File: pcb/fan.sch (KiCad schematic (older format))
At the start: 190 parts, among them J2 Pi, SW1 SW_PUSH, SW10 SW_PUSH, SW11 SW_PUSH, SW12 SW_PUSH, SW13 SW_PUSH, SW14 SW_PUSH, SW15 SW_PUSH, SW16 SW_PUSH, SW17 SW_PUSH, SW18 SW_PUSH, SW19 SW_PUSH, SW2 SW_PUSH, SW20 SW_PUSH, SW21 SW_PUSH, SW22 SW_PUSH, SW23 SW_PUSH, SW24 SW_PUSH, SW25 SW_PUSH, SW26 SW_PUSH, SW27 SW_PUSH, SW28 SW_PUSH, SW29 SW_PUSH, SW3 SW_PUSH, SW30 SW_PUSH, SW31 SW_PUSH, SW32 SW_PUSH, SW33 SW_PUSH, SW34 SW_PUSH, SW35 SW_PUSH, SW36 SW_PUSH, SW37 SW_PUSH, SW38 SW_PUSH, SW39 SW_PUSH, SW4 SW_PUSH, SW40 SW_PUSH, SW41 SW_PUSH, SW42 SW_PUSH, SW43 SW_PUSH, SW44 SW_PUSH, SW45 SW_PUSH, SW46 SW_PUSH, SW47 SW_PUSH, SW48 SW_PUSH, SW49 SW_PUSH, SW5 SW_PUSH, SW50 SW_PUSH, SW51 SW_PUSH, SW52 SW_PUSH, SW53 SW_PUSH, SW54 SW_PUSH, SW55 SW_PUSH, SW56 SW_PUSH, SW57 SW_PUSH, SW58 SW_PUSH, SW59 SW_PUSH, SW6 SW_PUSH, SW60 SW_PUSH, SW61 SW_PUSH, SW62 SW_PUSH, SW63 SW_PUSH, SW64 SW_PUSH, SW65 SW_PUSH, SW66 SW_PUSH, SW67 SW_PUSH, SW68 SW_PUSH, SW69 SW_PUSH, SW7 SW_PUSH, SW70 SW_PUSH, SW71 SW_PUSH, SW72 SW_PUSH, SW73 SW_PUSH, SW74 SW_PUSH, SW75 SW_PUSH, SW76 SW_PUSH, SW77 SW_PUSH, SW78 SW_PUSH, SW79 SW_PUSH, SW8 SW_PUSH, SW80 SW_PUSH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

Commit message: v2.0 外形考え中
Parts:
- removed D1, D10, D11, D12, D13, D14, D15, D16, D17, D18, D19, D2, D20, D21, D22, D23, D24, D25, D26, D27, D28, D29, D3, D30, D31, D32, D33, D34, D35, D36, D37, D38, D39, D4, D40, D41, D42, D43, D44, D45, D46, D47, D48, D49, D5, D50, D51, D52, D53, D54, D55, D56, D57, D58, D59, D6, D60, D61, D62, D63, D64, D65, D66, D67, D68, D69, D7, D70, D71, D72, D73, D74, D75, D76, D77, D78, D79, D8, D80, D81, D82, D83, D84, D85, D86, D87, D88, D89, D9, D90: DIODE, kbd:D3_TH_SMD, symbol Device:D
- removed J2: Pi, Connector_PinSocket_2.54mm:PinSocket_2x20_P2.54mm_Vertical, symbol fan-rescue:Connector_Generic_Conn_02x20_Odd_Even-Raspberry_Pi_Zero_W-cache
- removed SW1, SW10, SW11, SW12, SW13, SW14, SW15, SW16, SW17, SW18, SW19, SW2, SW20, SW21, SW22, SW23, SW24, SW25, SW26, SW27, SW28, SW29, SW3, SW30, SW31, SW32, SW33, SW34, SW35, SW36, SW37, SW38, SW39, SW4, SW40, SW41, SW42, SW43, SW44, SW45, SW46, SW47, SW48, SW5, SW51, SW52, SW53, SW54, SW56, SW57, SW58, SW59, SW6, SW60, SW61, SW62, SW63, SW64, SW65, SW66, SW67, SW68, SW69, SW7, SW70, SW71, SW72, SW73, SW74, SW75, SW76, SW77, SW78, SW79, SW8, SW80, SW81, SW82, SW83, SW84, SW85, SW86, SW87, SW88, SW89, SW9, SW90: SW_PUSH, kbd:CherryMX_Hotswap, symbol fan-rescue:SW_PUSH-kbd
- removed SW49, SW50, SW55: SW_PUSH, kbd:ResetSW, symbol fan-rescue:SW_PUSH-kbd
- removed SW93: SW_SPDT, Button_Switch_THT:SW_Slide_1P2T_CK_OS102011MS2Q, symbol Switch:SW_SPDT
- removed U4, U6: 74HC595, kbd:SN74HC595_DIP-16_W7.62mm_Socket_2, symbol 74xx:74HC595
- added SW1, SW11, SW12, SW13, SW14, SW16, SW17, SW18, SW19, SW2, SW20, SW21, SW22, SW23, SW24, SW25, SW26, SW27, SW28, SW29, SW3, SW30, SW31, SW32, SW33, SW34, SW35, SW36, SW37, SW38, SW39, SW4, SW40, SW6, SW7, SW8, SW9: SW_PUSH-kbd, kbd:CherryMX_MidHeight_Hotswap_edit, symbol New_Library:SW_PUSH-kbd
- added SW10, SW15, SW5: SW_PUSH-kbd, kbd:ResetSW_with_diode, symbol New_Library:SW_PUSH-kbd
- renumbered SW91 to SW41, SW92 to SW42
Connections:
- net labels removed: QHSER, QHSER', col08, col09, col10, col11, col12, col13, col14, row05
- wire segments 182 -> 80
- no-connect marks 58 -> 20

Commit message: 基盤の外形を決定した
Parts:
- added J1: MJ-4PP-9, kbd:MJ-4PP-9, symbol kbd:MJ-4PP-9
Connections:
- net labels added: data
- wire segments 80 -> 85
- no-connect marks 20 -> 18

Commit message: fan74をbluepillに変更
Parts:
- removed U1, U2: ProMicro, kbd:ProMicro_v3.6, symbol fan-rescue:ProMicro-kbd
- removed U3, U5: 74HC595, kbd:SN74HC595_DIP-16_W7.62mm_Socket_2, symbol 74xx:74HC595
- added R1: R, Resistor_THT:R_Axial_Power_L20.0mm_W6.4mm_P22.40mm, symbol Device:R
- added U1, U2: BluePill_STM32F103C, BluePill_breakouts:BluePill_STM32F103C, symbol bluepill_breakouts:BluePill_STM32F103C
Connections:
- net labels removed: OE, RCK, SCK, SCL, SER
- no-connect marks 18 -> 45
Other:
- moved on the sheet: SW42

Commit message: 配線にちょっと詰まったのでやり直す
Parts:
- added R10, R11, R12, R2, R20, R3, R4, R5, R6, R7, R8, R9: 10K, keyboard_parts:R_1608_rev2, symbol Device:R
- R1: value R -> 10K; footprint Resistor_THT:R_Axial_Power_L20.0mm_W6.4mm_P22.40mm -> keyboard_parts:R_1608_rev2
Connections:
- net data is gone; now on net Tx: J1.B
- net software_reset is gone; now on net hardware_reset: SW41.1
- net GND: now also SW42.1, U1.19 (GND), U1.20 (GND), U1.39 (GND), U2.19 (GND), U2.20 (GND), U2.39 (GND)
- net VCC: now also R1.2, U1.18 (VCC3V3), U1.40 (VCC3V3), U2.18 (VCC3V3), U2.40 (VCC3V3), R10.1, R11.1, R12.1, R2.1, R3.1, R4.1, R5.1, R6.1, R7.1, R8.1, R9.1; no longer R1.1
- net col01: now also U1.11 (PA6_MISO1), U2.11 (PA6_MISO1)
- net col02: now also U1.10 (PA5_SCK1), U2.10 (PA5_SCK1)
- net col03: now also U1.9 (PA4), U2.9 (PA4)
- net col04: now also U1.8 (PA3_RX2), U2.8 (PA3_RX2)
- net col05: now also U1.7 (PA2_TX2), U2.7 (PA2_TX2)
- net col06: now also U1.6 (PA1), U2.6 (PA1)
- net col07: now also U1.5 (PA0), U2.5 (PA0)
- net hardware_reset: now also U1.17 (NRST), U2.17 (NRST), R11.2; no longer SW42.1
- net row00: now also U1.33 (PB5), U2.33 (PB5)
- net row01: now also U1.34 (PB6_SCL1), U2.34 (PB6_SCL1)
- net row02: now also U1.35 (PB7_SDA1), U2.35 (PB7_SDA1)
- net row03: now also U1.36 (PB8), U2.36 (PB8)
- net row04: now also U1.37 (PB9), U2.37 (PB9)
- net at SW42.2: now also R12.2; no longer R1.2
- net PA7_R: now reaches U1.12 (PA7_MOSI1)
- net PA7_R: now also R1.1, U2.12 (PA7_MOSI1)
- net PB0_R: now reaches U1.13 (PB0)
- net PB0_R: now also U2.13 (PB0), R2.2
- net PB1_R: now reaches U1.14 (PB1)
- net PB1_R: now also U2.14 (PB1), R3.2
- net PB10_R: now reaches U1.15 (PB10_SCL2)
- net PB10_R: now also U2.15 (PB10_SCL2), R4.2
- net PB11_R: now reaches U1.16 (PB11_SDA2)
- net PB11_R: now also U2.16 (PB11_SDA2), R5.2
- net PB13_R: now reaches U1.22 (PB13_SCK2)
- net PB13_R: now also U2.22 (PB13_SCK2), R9.2
- net PB14_R: now reaches U1.23 (PB14_MISO2)
- net PB14_R: now also U2.23 (PB14_MISO2), R8.2
- net PB15_R: now reaches U1.24 (PB15_MOSI2)
- net PB15_R: now also U2.24 (PB15_MOSI2), R7.2
- net PA8_R: now reaches U1.25 (PA8)
- net PA8_R: now also U2.25 (PA8), R6.2
- net Tx: now reaches U1.26 (PA9_TX1)
- net Tx: now also U2.26 (PA9_TX1), R10.2, R20.1
- net Rx: now reaches U1.27 (PA10_RX1)
- net Rx: now also U2.27 (PA10_RX1), R20.2
- no-connect marks 45 -> 27
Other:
- moved on the sheet: J1, SW41, SW42, U1, U2

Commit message: fan74のPCBが一応完成した
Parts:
- removed R1, R12, R2, R20, R3, R4, R5, R6, R7, R8: 10K, keyboard_parts:R_1608_rev2, symbol Device:R
- removed SW42: SW_PUSH, kbd:ResetSW, symbol fan-rescue:SW_PUSH-kbd
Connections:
- net PA7_R is gone; now on net col00: U1.12 (PA7_MOSI1), U2.12 (PA7_MOSI1)
- net PB0_R is gone; now on net col04: U1.13 (PB0), U2.13 (PB0)
- net PB1_R is gone; now on net col05: U1.14 (PB1), U2.14 (PB1)
- net Rx: now also R9.2
- net Tx: now also R9.1
- net VCC: no longer R9.1
- net col01: now also U1.9 (PA4), U2.9 (PA4); no longer U1.11 (PA6_MISO1), U2.11 (PA6_MISO1)
- net col03: now also U1.11 (PA6_MISO1), U2.11 (PA6_MISO1); no longer U1.9 (PA4), U2.9 (PA4)
- net col04: no longer U1.8 (PA3_RX2), U2.8 (PA3_RX2)
- net col05: no longer U1.7 (PA2_TX2), U2.7 (PA2_TX2)
- net row00: now also U1.37 (PB9), U2.37 (PB9); no longer U1.33 (PB5), U2.33 (PB5)
- net row01: now also U1.36 (PB8), U2.36 (PB8); no longer U1.34 (PB6_SCL1), U2.34 (PB6_SCL1)
- net row03: now also U1.34 (PB6_SCL1), U2.34 (PB6_SCL1); no longer U1.36 (PB8), U2.36 (PB8)
- net row04: now also U1.33 (PB5), U2.33 (PB5); no longer U1.37 (PB9), U2.37 (PB9)
- net PA8_R: no longer names the net of U1.25 (PA8)
- net PA8_R: no longer U2.25 (PA8)
- net PB10_R: no longer names the net of U1.15 (PB10_SCL2)
- net PB10_R: no longer U2.15 (PB10_SCL2)
- net PB11_R: no longer names the net of U1.16 (PB11_SDA2)
- net PB11_R: no longer U2.16 (PB11_SDA2)
- removed net PB13_R: R9.2, U1.22 (PB13_SCK2), U2.22 (PB13_SCK2)
- net PB14_R: no longer names the net of U1.23 (PB14_MISO2)
- net PB14_R: no longer U2.23 (PB14_MISO2)
- net PB15_R: no longer names the net of U1.24 (PB15_MOSI2)
- net PB15_R: no longer U2.24 (PB15_MOSI2)
- no-connect marks 27 -> 43

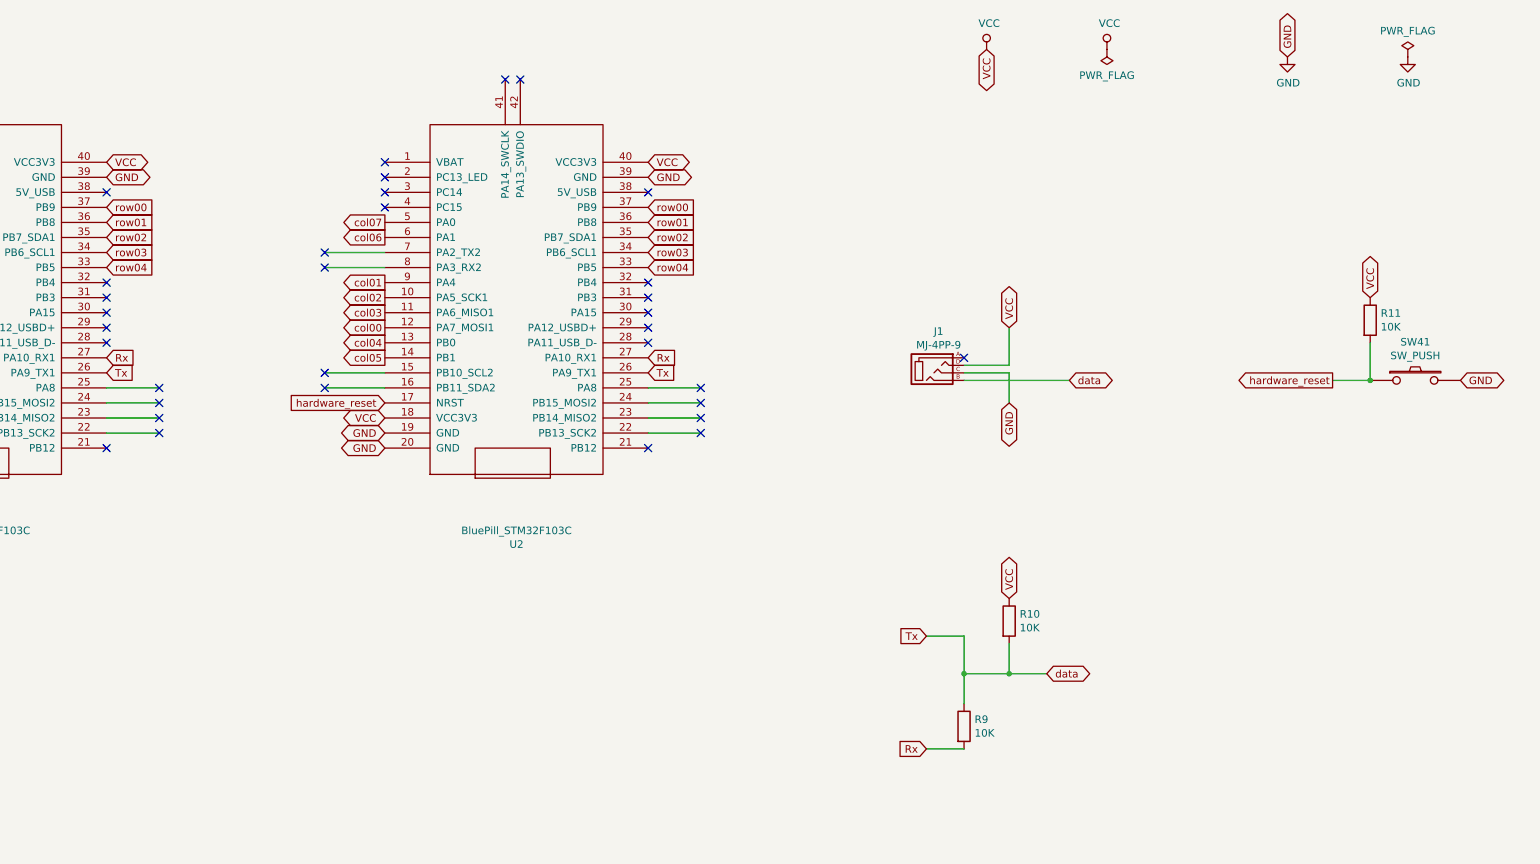
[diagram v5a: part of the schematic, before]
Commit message: fan74のケースを作成
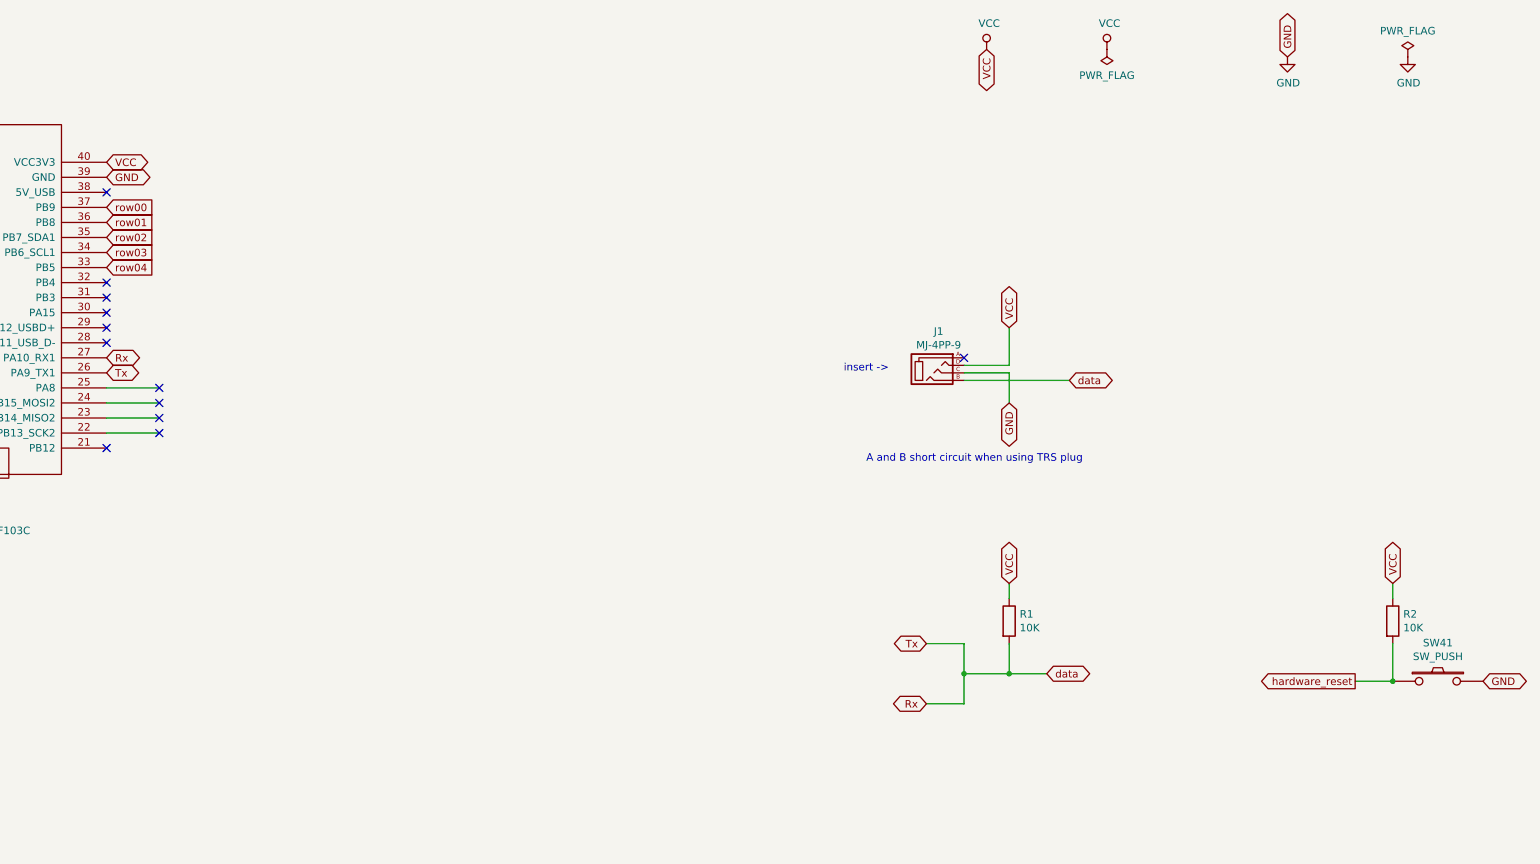
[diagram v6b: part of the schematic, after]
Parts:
- removed R9: 10K, keyboard_parts:R_1608_rev2, symbol Device:R
- removed U2: BluePill_STM32F103C, BluePill_breakouts:BluePill_STM32F103C, symbol bluepill_breakouts:BluePill_STM32F103C
- U1: footprint BluePill_breakouts:BluePill_STM32F103C -> BluePill_breakouts:BluePill_STM32F103C_0.9_Double
- renumbered R10 to R1, R11 to R2
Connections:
- net Tx is gone; now on net Rx: J1.B, R1.2, U1.26 (PA9_TX1)
- no-connect marks 43 -> 22
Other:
- note added: "A and B short circuit when using TRS plug"
- note added: "insert ->"
- moved on the sheet: R2, SW41
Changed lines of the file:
@@
 Text GLabel 2600 4100 0    50   Input ~ 0
 hardware_reset
-Text GLabel 12500 3950 0    50   Output ~ 0
+Text GLabel 12650 5950 0    50   Output ~ 0
 hardware_reset
 Wire Wire Line
@@
 NoConn ~ 3400 1950
 NoConn ~ 3500 1950
-NoConn ~ 7100 1950
 Text GLabel 2600 4200 0    50   BiDi ~ 0
 VCC
-NoConn ~ 7000 1950
 $Comp
 L power:VCC #PWR0103
@@
 L fan-rescue:SW_PUSH-kbd SW41
 U 1 1 5E845F2A
-P 13050 3950
-F 0 "SW41" H 13050 4205 50  0000 C CNN
-F 1 "SW_PUSH" H 13050 4114 50  0000 C CNN
-F 2 "kbd:ResetSW" H 13050 3950 50  0001 C CNN
-F 3 "" H 13050 3950 50  0000 C CNN
-	1    13050 3950
-	1    0    0    -1
-$EndComp
-$Comp
-L bluepill_breakouts:BluePill_STM32F103C U2
-U 1 1 5E74A9F6
-P 7050 3400
-F 0 "U2" H 7025 5040 50  0000 C CNN
-F 1 "BluePill_STM32F103C" H 7025 4949 50  0000 C CNN
-F 2 "BluePill_breakouts:BluePill_STM32F103C" H 7100 1800 50  0001 C CNN
-F 3 "www.rogerclark.net" H 7050 1900 50  0001 C CNN
-	1    7050 3400
-	-1   0    0    1
+P 13200 5950
+F 0 "SW41" H 13200 6205 50  0000 C CNN
+F 1 "SW_PUSH" H 13200 6114 50  0000 C CNN
+F 2 "kbd:ResetSW" H 13200 5950 50  0001 C CNN
+F 3 "" H 13200 5950 50  0000 C CNN
+	1    13200 5950
+	1    0    0    -1
 $EndComp
 Text GLabel 4350 2500 2    50   BiDi ~ 0
@@
 F 0 "U1" H 3425 5040 50  0000 C CNN
 F 1 "BluePill_STM32F103C" H 3425 4949 50  0000 C CNN
-F 2 "BluePill_breakouts:BluePill_STM32F103C" H 3500 1800 50  0001 C CNN
+F 2 "BluePill_breakouts:BluePill_STM32F103C_0.9_Double" H 3500 1800 50  0001 C CNN
 F 3 "www.rogerclark.net" H 3450 1900 50  0001 C CNN
 	1    3450 3400
 	-1   0    0    1
 $EndComp
-Text GLabel 4350 3900 2    50   Input ~ 0
+Text GLabel 4350 3900 2    50   BiDi ~ 0
 Tx
-Text GLabel 4350 3800 2    50   Input ~ 0
+Text GLabel 4350 3800 2    50   BiDi ~ 0
 Rx
 NoConn ~ 2600 2600
@@
 NoConn ~ 4350 3500
 NoConn ~ 4350 3300
-Text GLabel 13350 3950 2    50   BiDi ~ 0
+Text GLabel 13500 5950 2    50   BiDi ~ 0
 GND
 Wire Wire Line
-	12500 3950 12750 3950
-Text GLabel 12750 3400 1    50   BiDi ~ 0
-VCC
-Wire Wire Line
-	12750 3700 12750 3950
-Connection ~ 12750 3950
+	12650 5950 12900 5950
+Wire Wire Line
+	12900 5700 12900 5950
+Connection ~ 12900 5950
 NoConn ~ 2600 2800
 NoConn ~ 2600 2500
-Text GLabel 9800 5650 0    50   Input ~ 0
-Tx
-Text GLabel 9800 6400 0    50   Input ~ 0
-Rx
-Wire Wire Line
-	9800 5650 10050 5650
-Wire Wire Line
-	10050 6400 9800 6400
-Wire Wire Line
-	10050 5650 10050 5900
+Wire Wire Line
+	9800 5700 10050 5700
 Wire Wire Line
 	10600 5900 10350 5900
 Connection ~ 10050 5900
-Wire Wire Line
-	10050 5900 10050 6100
 NoConn ~ 4350 2700
-Text GLabel 7950 2600 2    50   BiDi ~ 0
-GND
-Text GLabel 6200 4400 0    50   BiDi ~ 0
-GND
-Text GLabel 6200 4300 0    50   BiDi ~ 0
-GND
-Text GLabel 6200 4200 0    50   BiDi ~ 0
-VCC
-Text GLabel 7950 2500 2    50   BiDi ~ 0
-VCC
-Text GLabel 7950 3900 2    50   Input ~ 0
-Tx
-Text GLabel 7950 3800 2    50   Input ~ 0
-Rx
-NoConn ~ 6200 2600
-NoConn ~ 7950 4400
-NoConn ~ 7950 3700
-NoConn ~ 7950 3600
-NoConn ~ 7950 3400
-NoConn ~ 7950 3500
-NoConn ~ 7950 3300
-NoConn ~ 6200 2800
-NoConn ~ 6200 2500
-NoConn ~ 7950 2700
 NoConn ~ 2600 2700
-NoConn ~ 6200 2700
 Wire Wire Line
 	10350 5700 10350 5900
 Wire Wire Line
 	10050 3950 10750 3950
-Text GLabel 10350 5400 1    50   BiDi ~ 0
+Text GLabel 10350 5300 1    50   BiDi ~ 0
 VCC
 Connection ~ 10350 5900
@@
 Wire Wire Line
 	4350 4300 4700 4300
-Wire Wire Line
-	7950 4000 8300 4000
-Wire Wire Line
-	7950 4100 8300 4100
-Wire Wire Line
-	7950 4200 8300 4200
-Wire Wire Line
-	7950 4300 8300 4300
-Wire Wire Line
-	6200 3900 5800 3900
-Wire Wire Line
-	6200 4000 5800 4000
-Text GLabel 7950 3200 2    50   Input ~ 0
-row04
-Text GLabel 7950 3100 2    50   Input ~ 0
-row03
-Text GLabel 7950 2800 2    50   Input ~ 0
-row00
-Text GLabel 7950 2900 2    50   Input ~ 0
-row01
-Text GLabel 7950 3000 2    50   Input ~ 0
-row02
 Text GLabel 2600 2900 0    50   Output ~ 0
 col07
@@
 Text GLabel 2600 3600 0    50   Output ~ 0
 col00
-Text GLabel 6200 3000 0    50   Output ~ 0
-col06
-Text GLabel 6200 2900 0    50   Output ~ 0
-col07
-Wire Wire Line
-	6200 3100 5800 3100
-Wire Wire Line
-	6200 3200 5800 3200
-Text GLabel 6200 3800 0    50   Output ~ 0
-col05
-Text GLabel 6200 3500 0    50   Output ~ 0
-col03
-Text GLabel 6200 3700 0    50   Output ~ 0
-col04
-Text GLabel 6200 3300 0    50   Output ~ 0
-col01
-Text GLabel 6200 3400 0    50   Output ~ 0
-col02
-Text GLabel 6200 3600 0    50   Output ~ 0
-col00
-$Comp
-L Device:R R9
-U 1 1 5EC7C591
-P 10050 6250
-F 0 "R9" H 10120 6296 50  0000 L CNN
-F 1 "10K" H 10120 6205 50  0000 L CNN
-F 2 "keyboard_parts:R_1608_rev2" V 9980 6250 50  0001 C CNN
-F 3 "~" H 10050 6250 50  0001 C CNN
-	1    10050 6250
-	1    0    0    -1
-$EndComp
-$Comp
-L Device:R R10
+$Comp
+L Device:R R1
 U 1 1 5EC895B1
 P 10350 5550
-F 0 "R10" H 10420 5596 50  0000 L CNN
+F 0 "R1" H 10420 5596 50  0000 L CNN
 F 1 "10K" H 10420 5505 50  0000 L CNN
 F 2 "keyboard_parts:R_1608_rev2" V 10280 5550 50  0001 C CNN
@@
 $EndComp
 $Comp
-L Device:R R11
+L Device:R R2
 U 1 1 5EC8FA28
-P 12750 3550
-F 0 "R11" H 12820 3596 50  0000 L CNN
-F 1 "10K" H 12820 3505 50  0000 L CNN
-F 2 "keyboard_parts:R_1608_rev2" V 12680 3550 50  0001 C CNN
-F 3 "~" H 12750 3550 50  0001 C CNN
-	1    12750 3550
+P 12900 5550
+F 0 "R2" H 12970 5596 50  0000 L CNN
+F 1 "10K" H 12970 5505 50  0000 L CNN
+F 2 "keyboard_parts:R_1608_rev2" V 12830 5550 50  0001 C CNN
+F 3 "~" H 12900 5550 50  0001 C CNN
+	1    12900 5550
 	1    0    0    -1
 $EndComp
@@
 NoConn ~ 2200 3100
 NoConn ~ 2200 3200
-Text GLabel 6200 4100 0    50   Input ~ 0
-hardware_reset
-NoConn ~ 5800 3100
-NoConn ~ 5800 3200
-NoConn ~ 5800 3900
-NoConn ~ 5800 4000
-NoConn ~ 8300 4000
-NoConn ~ 8300 4100
-NoConn ~ 8300 4200
-NoConn ~ 8300 4300
+Wire Wire Line
+	10050 5900 10050 6100
+Wire Wire Line
+	10050 6100 9800 6100
+Text GLabel 9800 6100 0    50   BiDi ~ 0
+Rx
+Wire Wire Line
+	10050 5700 10050 5900
+Wire Wire Line
+	10350 5300 10350 5400
+Text GLabel 12900 5300 1    50   BiDi ~ 0
+VCC
+Wire Wire Line
+	12900 5400 12900 5300
+Text GLabel 9800 5700 0    50   BiDi ~ 0
+Tx
+Text Notes 9250 3900 0    50   ~ 0
+insert ->
+Text Notes 9400 4500 0    50   ~ 0
+A and B short circuit when using TRS plug
 $EndSCHEMATC

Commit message: 異種面付けしてみた がしないで3枚注文してもトントンだったので 普通に発注する予定
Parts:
- added J2, J3: Conn_01x01_Female, Connector_Pin:Pin_D1.0mm_L10.0mm, symbol Connector:Conn_01x01_Female
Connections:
- net at U1.7 (PA2_TX2): now also J2.1 (Pin_1)
- net at U1.8 (PA3_RX2): now also J3.1 (Pin_1)
- no-connect marks 22 -> 20
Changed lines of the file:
@@
 	10350 5900 10050 5900
-Wire Wire Line
-	2600 3100 2200 3100
-Wire Wire Line
-	2600 3200 2200 3200
 Wire Wire Line
 	2600 3900 2200 3900
@@
 NoConn ~ 2200 3900
 NoConn ~ 2200 4000
-NoConn ~ 2200 3100
-NoConn ~ 2200 3200
 Wire Wire Line
 	10050 5900 10050 6100
@@
 Text Notes 9400 4500 0    50   ~ 0
 A and B short circuit when using TRS plug
+Wire Wire Line
+	1850 3200 2600 3200
+Wire Wire Line
+	1850 3100 2600 3100
+$Comp
+L Connector:Conn_01x01_Female J2
+U 1 1 5E6E9A12
+P 1650 3100
+F 0 "J2" H 1542 2875 50  0000 C CNN
+F 1 "Conn_01x01_Female" H 1542 2966 50  0000 C CNN
+F 2 "Connector_Pin:Pin_D1.0mm_L10.0mm" H 1650 3100 50  0001 C CNN
+F 3 "~" H 1650 3100 50  0001 C CNN
+	1    1650 3100
+	-1   0    0    1
+$EndComp
+$Comp
+L Connector:Conn_01x01_Female J3
+U 1 1 5E6EAD64
+P 1650 3200
+F 0 "J3" H 1542 2975 50  0000 C CNN
+F 1 "Conn_01x01_Female" H 1542 3066 50  0000 C CNN
+F 2 "Connector_Pin:Pin_D1.0mm_L10.0mm" H 1650 3200 50  0001 C CNN
+F 3 "~" H 1650 3200 50  0001 C CNN
+	1    1650 3200
+	-1   0    0    1
+$EndComp
 $EndSCHEMATC
